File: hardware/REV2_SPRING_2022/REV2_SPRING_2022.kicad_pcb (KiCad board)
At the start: 2 copper layers, 105 x 250 mm, 54 parts, among them J101 Screw_Terminal_01x02, J102 Screw_Terminal_01x02, J103 Conn_01x02_Female, J104 Screw_Terminal_01x02, J105 Conn_01x02_Female, J107 Screw_Terminal_01x02, J109 Conn_01x02_Female, J110 Conn_01x02_Female, Q101 Q_NMOS_GDS, Q102 Q_NMOS_GDS, U1 Teensy3.6_All_Pins, U2 PA16165_Breakout, U201 TPS2113ADRBR, U3 MPL3115A2_Breakout, U301 TPS2113ADRBR, U4 BNO055_Breakout, U5 RFM69HCW_Breakout

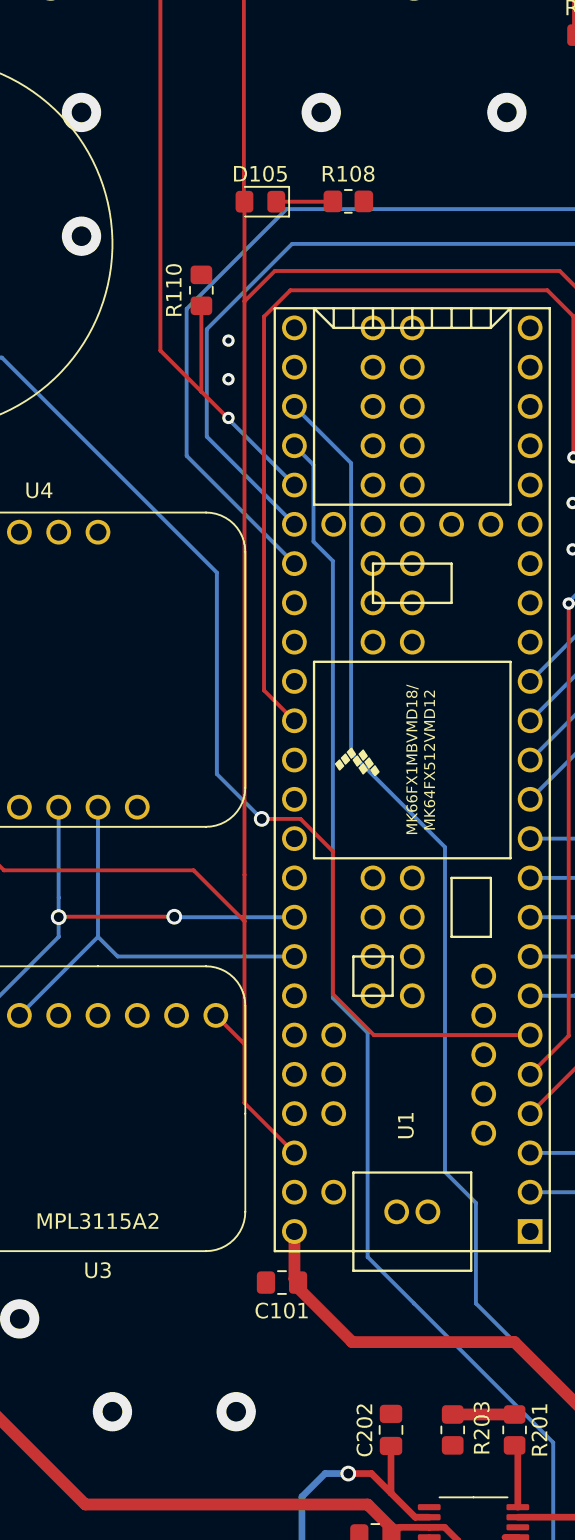
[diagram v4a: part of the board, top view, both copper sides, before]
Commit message: add pullup resistors on TPS stat pins
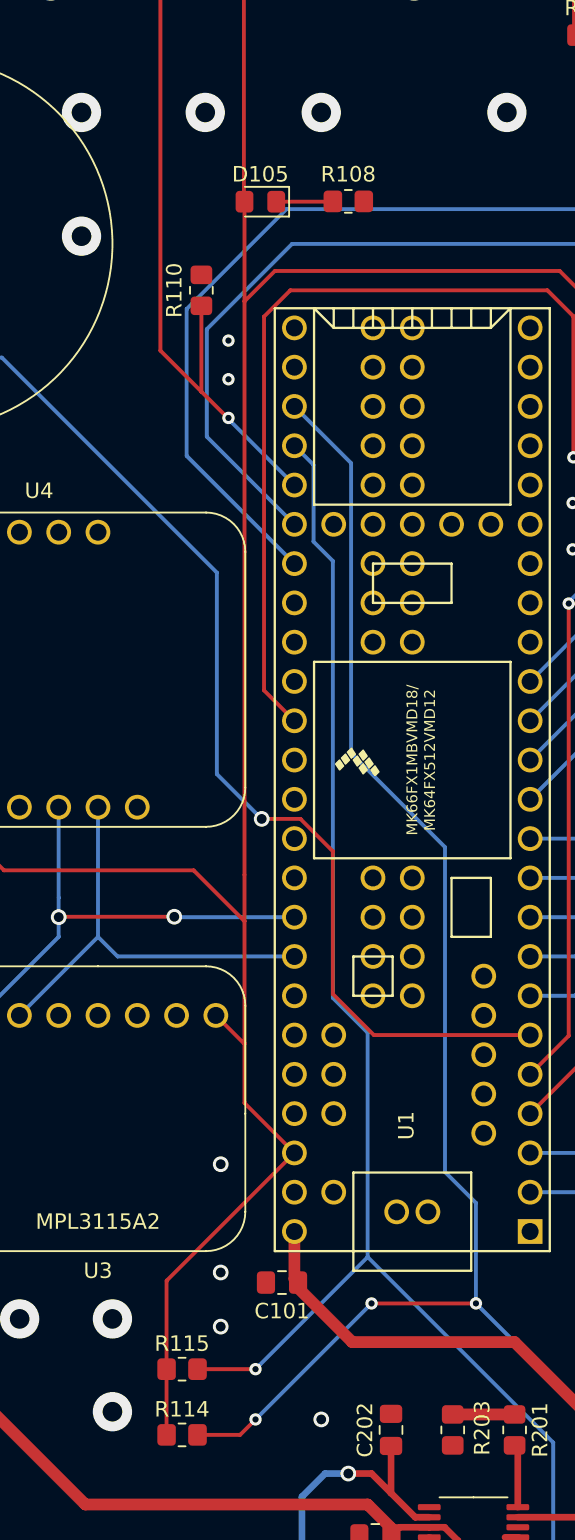
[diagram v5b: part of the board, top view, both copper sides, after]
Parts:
- added R114: R_10k, Resistor_SMD:R_0805_2012Metric_Pad1.20x1.40mm_HandSolder, F.Cu at (95.0, 162.0)
- added R115: R_10k, Resistor_SMD:R_0805_2012Metric_Pad1.20x1.40mm_HandSolder, F.Cu at (95.0, 157.8)
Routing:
- net /3.3V: track 249.5 -> 271.2 mm
- net /TPS_1_STAT: track 103.6 -> 125.1 mm, vias 1 -> 4
- net /TPS_2_STAT: track 90.2 -> 104.2 mm, vias 1 -> 2
- net GND: vias 211 -> 216
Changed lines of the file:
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@@
     (thickness 1.6)
     (drawings 38)
-    (tracks 549)
+    (tracks 569)
     (zones 0)
-    (modules 54)
+    (modules 56)
     (nets 126)
   )
@@
     )
   )
+  (module Resistor_SMD:R_0805_2012Metric_Pad1.20x1.40mm_HandSolder (layer F.Cu)
+    (at 95 162)
+    (descr "Resistor SMD 0805 (2012 Metric), square (rectangular) end terminal, IPC_7351 nominal with elongated pad for handsoldering. (Body size source: IPC-SM-782 page 72, https://www.pcb-3d.com/wordpress/wp-content/uploads/ipc-sm-782a_amendment_1_and_2.pdf), generated with kicad-footprint-generator")
+    (tags "resistor handsolder")
+    (attr smd)
+    (fp_text reference R114 (at 0 -1.65) (layer F.SilkS)
+      (effects (font (size 1 1) (thickness 0.15)))
+    )
+    (fp_text value R_10k (at 0 1.65) (layer F.Fab)
+      (effects (font (size 1 1) (thickness 0.15)))
+    )
+    (fp_text user %R (at 0 0) (layer F.Fab)
+      (effects (font (size 0.5 0.5) (thickness 0.08)))
+    )
+    (fp_line (start -1 0.625) (end -1 -0.625) (layer F.Fab) (width 0.1))
+    (fp_line (start -1 -0.625) (end 1 -0.625) (layer F.Fab) (width 0.1))
+    (fp_line (start 1 -0.625) (end 1 0.625) (layer F.Fab) (width 0.1))
+    (fp_line (start 1 0.625) (end -1 0.625) (layer F.Fab) (width 0.1))
+    (fp_line (start -0.227064 -0.735) (end 0.227064 -0.735) (layer F.SilkS) (width 0.12))
+    (fp_line (start -0.227064 0.735) (end 0.227064 0.735) (layer F.SilkS) (width 0.12))
+    (fp_line (start -1.85 0.95) (end -1.85 -0.95) (layer F.CrtYd) (width 0.05))
+    (fp_line (start -1.85 -0.95) (end 1.85 -0.95) (layer F.CrtYd) (width 0.05))
+    (fp_line (start 1.85 -0.95) (end 1.85 0.95) (layer F.CrtYd) (width 0.05))
+    (fp_line (start 1.85 0.95) (end -1.85 0.95) (layer F.CrtYd) (width 0.05))
+    (pad 2 smd roundrect (at 1 0) (size 1.2 1.4) (layers F.Cu F.Paste F.Mask) (roundrect_rratio 0.208333)
+      (net 19 /TPS_1_STAT))
+    (pad 1 smd roundrect (at -1 0) (size 1.2 1.4) (layers F.Cu F.Paste F.Mask) (roundrect_rratio 0.208333)
+      (net 11 /3.3V))
+    (model ${KISYS3DMOD}/Resistor_SMD.3dshapes/R_0805_2012Metric.wrl
+      (at (xyz 0 0 0))
+      (scale (xyz 1 1 1))
+      (rotate (xyz 0 0 0))
+    )
+  )
+  (module Resistor_SMD:R_0805_2012Metric_Pad1.20x1.40mm_HandSolder (layer F.Cu)
+    (at 95 157.75)
+    (descr "Resistor SMD 0805 (2012 Metric), square (rectangular) end terminal, IPC_7351 nominal with elongated pad for handsoldering. (Body size source: IPC-SM-782 page 72, https://www.pcb-3d.com/wordpress/wp-content/uploads/ipc-sm-782a_amendment_1_and_2.pdf), generated with kicad-footprint-generator")
+    (tags "resistor handsolder")
+    (attr smd)
+    (fp_text reference R115 (at 0 -1.65) (layer F.SilkS)
+      (effects (font (size 1 1) (thickness 0.15)))
+    )
+    (fp_text value R_10k (at 0 1.65) (layer F.Fab)
+      (effects (font (size 1 1) (thickness 0.15)))
+    )
+    (fp_line (start 1.85 0.95) (end -1.85 0.95) (layer F.CrtYd) (width 0.05))
+    (fp_line (start 1.85 -0.95) (end 1.85 0.95) (layer F.CrtYd) (width 0.05))
+    (fp_line (start -1.85 -0.95) (end 1.85 -0.95) (layer F.CrtYd) (width 0.05))
+    (fp_line (start -1.85 0.95) (end -1.85 -0.95) (layer F.CrtYd) (width 0.05))
+    (fp_line (start -0.227064 0.735) (end 0.227064 0.735) (layer F.SilkS) (width 0.12))
+    (fp_line (start -0.227064 -0.735) (end 0.227064 -0.735) (layer F.SilkS) (width 0.12))
+    (fp_line (start 1 0.625) (end -1 0.625) (layer F.Fab) (width 0.1))
+    (fp_line (start 1 -0.625) (end 1 0.625) (layer F.Fab) (width 0.1))
+    (fp_line (start -1 -0.625) (end 1 -0.625) (layer F.Fab) (width 0.1))
+    (fp_line (start -1 0.625) (end -1 -0.625) (layer F.Fab) (width 0.1))
+    (fp_text user %R (at 0 0) (layer F.Fab)
+      (effects (font (size 0.5 0.5) (thickness 0.08)))
+    )
+    (pad 1 smd roundrect (at -1 0) (size 1.2 1.4) (layers F.Cu F.Paste F.Mask) (roundrect_rratio 0.208333)
+      (net 11 /3.3V))
+    (pad 2 smd roundrect (at 1 0) (size 1.2 1.4) (layers F.Cu F.Paste F.Mask) (roundrect_rratio 0.208333)
+      (net 17 /TPS_2_STAT))
+    (model ${KISYS3DMOD}/Resistor_SMD.3dshapes/R_0805_2012Metric.wrl
+      (at (xyz 0 0 0))
+      (scale (xyz 1 1 1))
+      (rotate (xyz 0 0 0))
+    )
+  )
   (gr_text "DROGUE\nEMATCH" (at 143.25 42.25) (layer F.SilkS)
     (effects (font (size 1.5 1.5) (thickness 0.3)))
@@
   (segment (start 99.037 128.787) (end 99.037 125.787) (width 0.25) (layer F.Cu) (net 11))
   (segment (start 99.037 136.713) (end 99.037 128.787) (width 0.25) (layer F.Cu) (net 11))
+  (segment (start 94 162) (end 94 157.75) (width 0.25) (layer F.Cu) (net 11))
+  (segment (start 94 152.034) (end 102.265 143.769) (width 0.25) (layer F.Cu) (net 11))
+  (segment (start 94 157.75) (end 94 152.034) (width 0.25) (layer F.Cu) (net 11))
   (segment (start 73.555 188.72) (end 73.555 186.055) (width 1.524) (layer F.Cu) (net 12))
   (segment (start 73.555 186.055) (end 73.5 186) (width 1.524) (layer F.Cu) (net 12))
@@
   (via (at 78.5 148.5) (size 2.54) (drill 1.27) (layers F.Cu B.Cu) (net 12))
   (via (at 84.5 154.5) (size 2.54) (drill 1.27) (layers F.Cu B.Cu) (net 12))
-  (via (at 90.5 160.5) (size 2.54) (drill 1.27) (layers F.Cu B.Cu) (net 12))
-  (via (at 98.5 160.5) (size 2.54) (drill 1.27) (layers F.Cu B.Cu) (net 12))
   (via (at 80.5 168.5) (size 2.54) (drill 1.27) (layers F.Cu B.Cu) (net 12))
   (via (at 74.5 162.5) (size 2.54) (drill 1.27) (layers F.Cu B.Cu) (net 12))
@@
   (via (at 158 202) (size 2.54) (drill 1.27) (layers F.Cu B.Cu) (net 12))
   (via (at 158 218) (size 2.54) (drill 1.27) (layers F.Cu B.Cu) (net 12))
+  (via (at 90.5 160.5) (size 2.54) (drill 1.27) (layers F.Cu B.Cu) (net 12))
+  (via (at 97.5 151.5) (size 1.016) (drill 0.635) (layers F.Cu B.Cu) (net 12))
+  (via (at 97.5 155) (size 1.016) (drill 0.635) (layers F.Cu B.Cu) (net 12))
+  (via (at 97.5 144.5) (size 1.016) (drill 0.635) (layers F.Cu B.Cu) (net 12))
+  (via (at 90.5 154.5) (size 2.54) (drill 1.27) (layers F.Cu B.Cu) (net 12))
+  (via (at 104 161) (size 1.016) (drill 0.635) (layers F.Cu B.Cu) (net 12))
+  (via (at 96.5 76.5) (size 2.54) (drill 1.27) (layers F.Cu B.Cu) (net 12))
   (segment (start 117.5 63.15) (end 120.6 66.25) (width 1.524) (layer F.Cu) (net 13) (status 20))
   (segment (start 117.5 27.42) (end 117.5 63.15) (width 1.524) (layer F.Cu) (net 13))
@@
   (segment (start 103.5 99.284) (end 103.5 104.25) (width 0.25) (layer B.Cu) (net 17))
   (segment (start 102.265 98.049) (end 103.5 99.284) (width 0.25) (layer B.Cu) (net 17))
+  (segment (start 107 150.5) (end 100 157.5) (width 0.25) (layer B.Cu) (net 17))
+  (via (at 99.75 157.75) (size 0.8) (drill 0.4) (layers F.Cu B.Cu) (net 17))
+  (segment (start 100 157.5) (end 99.75 157.75) (width 0.25) (layer B.Cu) (net 17))
+  (segment (start 99.75 157.75) (end 96 157.75) (width 0.25) (layer F.Cu) (net 17))
   (segment (start 138.2665 165.275) (end 136.765 166.7765) (width 0.4318) (layer F.Cu) (net 18) (status 20))
   (segment (start 139.951 165.275) (end 138.2665 165.275) (width 0.4318) (layer F.Cu) (net 18) (status 10))
@@
   (segment (start 121.5 170.5) (end 121.5 161.000006) (width 0.25) (layer B.Cu) (net 19))
   (segment (start 121.5 161.000006) (end 114 153.500006) (width 0.25) (layer B.Cu) (net 19))
+  (via (at 114 153.500006) (size 0.8) (drill 0.4) (layers F.Cu B.Cu) (net 19))
+  (segment (start 114 153.500006) (end 114 153.5) (width 0.25) (layer F.Cu) (net 19))
+  (via (at 107.25 153.5) (size 0.8) (drill 0.4) (layers F.Cu B.Cu) (net 19))
+  (segment (start 114 153.5) (end 107.25 153.5) (width 0.25) (layer F.Cu) (net 19))
+  (via (at 99.75 161) (size 0.8) (drill 0.4) (layers F.Cu B.Cu) (net 19))
+  (segment (start 107.25 153.5) (end 99.75 161) (width 0.25) (layer B.Cu) (net 19))
+  (segment (start 98.75 162) (end 96 162) (width 0.25) (layer F.Cu) (net 19))
+  (segment (start 99.75 161) (end 98.75 162) (width 0.25) (layer F.Cu) (net 19))
   (via (at 157.5 134) (size 0.8) (drill 0.4) (layers F.Cu B.Cu) (net 20))
   (segment (start 160.975 134) (end 161 134.025) (width 0.25) (layer F.Cu) (net 20))
